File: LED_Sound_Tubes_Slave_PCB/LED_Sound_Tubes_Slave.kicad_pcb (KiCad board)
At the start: 2 copper layers, 111.9 x 52.1 mm, 50 parts, among them IC1 4050D, J2 Teensy_3_2_Header, P1 POWER + DATA, P10 LED_STR_4, P11 LED_STR_5, P2 +5V, P3 0V, P4 +5V, P5 0V, P6 LED_STR_1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

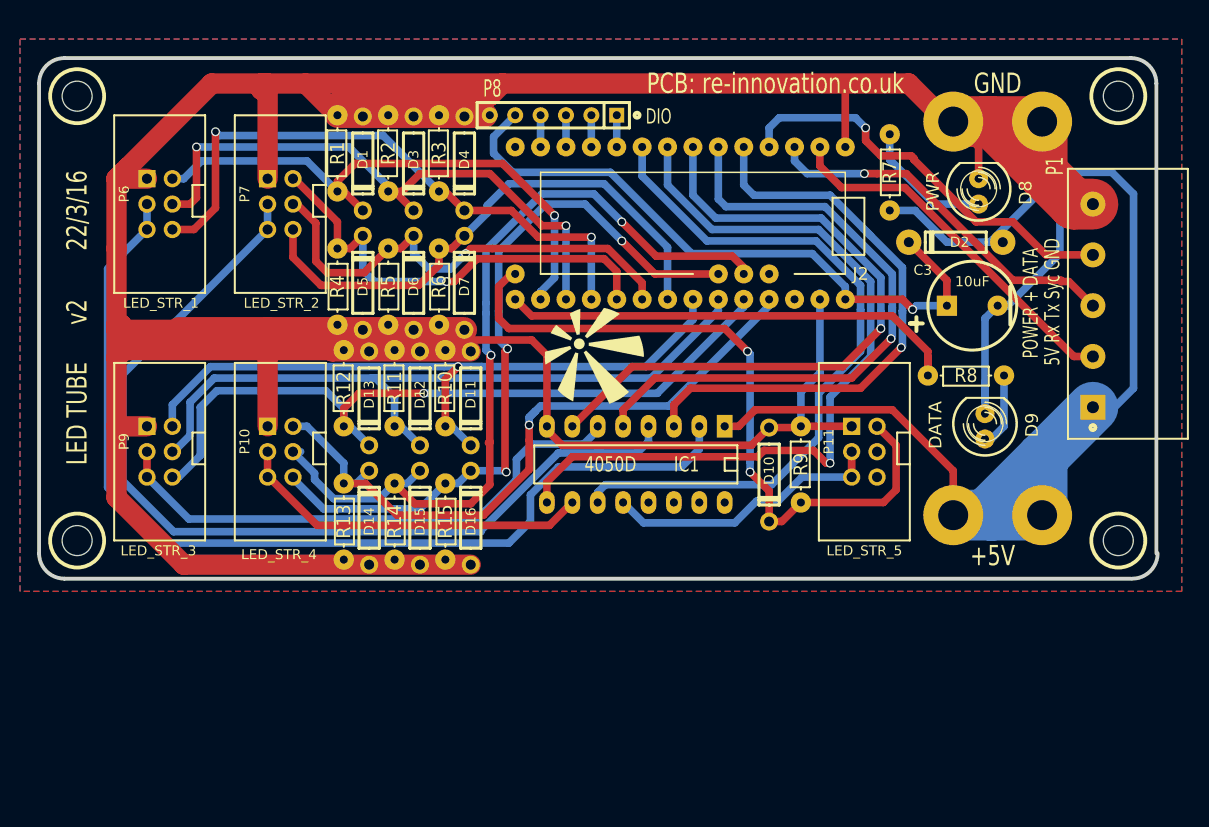
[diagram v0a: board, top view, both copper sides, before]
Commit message: New PCB with filters
Added filters. Total redesign of PCB
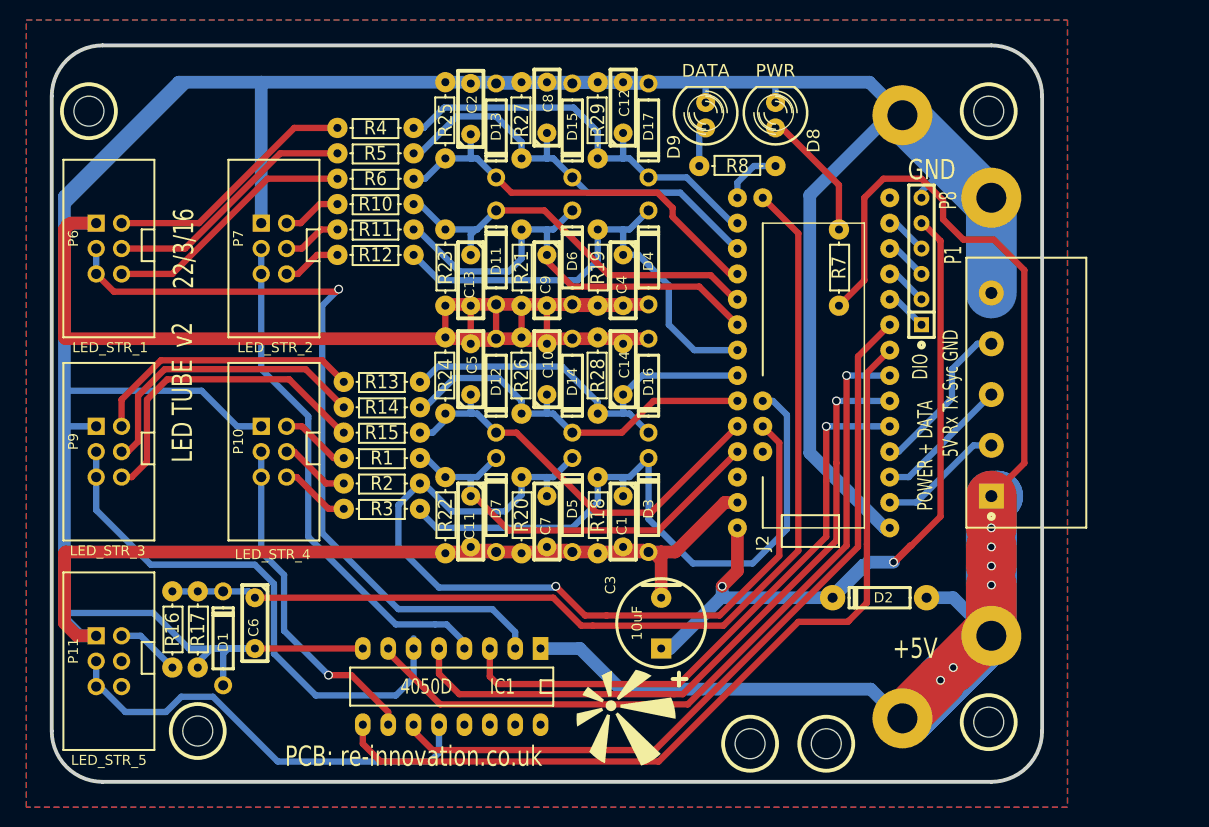
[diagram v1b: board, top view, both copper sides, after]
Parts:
- removed D10: 5V1 Diode, REInnovationFootprint:TH_Diode_3
- removed R9: 1M, REInnovationFootprint:TH_Resistor_1
- added C1: 100n, matts_components:C1_wide_lg_pad, F.Cu at (138.4, 104.8)
- added C10: 100n, matts_components:C1_wide_lg_pad, F.Cu at (130.8, 92.1)
- added C11: 100n, matts_components:C1_wide_lg_pad, F.Cu at (123.2, 104.8)
- added C12: 100n, matts_components:C1_wide_lg_pad, F.Cu at (138.4, 65.9)
- added C13: 100n, matts_components:C1_wide_lg_pad, F.Cu at (123.2, 80.6)
- added C14: 100n, matts_components:C1_wide_lg_pad, F.Cu at (138.4, 92.1)
- added C2: 100n, matts_components:C1_wide_lg_pad, F.Cu at (123.2, 66.0)
- added C4: 100n, matts_components:C1_wide_lg_pad, F.Cu at (138.4, 80.6)
- added C5: 100n, matts_components:C1_wide_lg_pad, F.Cu at (123.2, 92.1)
- added C6: 100n, matts_components:C1_wide_lg_pad, F.Cu at (101.6, 114.9)
- added C7: 100n, matts_components:C1_wide_lg_pad, F.Cu at (130.8, 104.8)
- added C8: 100n, matts_components:C1_wide_lg_pad, F.Cu at (130.8, 65.9)
- added C9: 100n, matts_components:C1_wide_lg_pad, F.Cu at (130.8, 80.6)
- added D17: 5V1 Diode, REInnovationFootprint:TH_Diode_3, F.Cu at (141.0, 66.5)
- added MH5: CONN_1, REInnovationFootprint:3mm_hole, F.Cu at (158.8, 128.3)
- added MH6: CONN_1, REInnovationFootprint:3mm_hole, F.Cu at (151.1, 128.3)
- added R16: 1k, REInnovationFootprint:TH_Resistor_1, F.Cu at (93.3, 116.8)
- added R17: 1M, REInnovationFootprint:TH_Resistor_1, F.Cu at (95.9, 116.8)
- added R18: 1M, REInnovationFootprint:TH_Resistor_1, F.Cu at (135.9, 105.4)
- added R19: 1M, REInnovationFootprint:TH_Resistor_1, F.Cu at (135.9, 80.6)
- added R20: 1M, REInnovationFootprint:TH_Resistor_1, F.Cu at (128.3, 105.4)
- added R21: 1M, REInnovationFootprint:TH_Resistor_1, F.Cu at (128.3, 80.6)
- added R22: 1M, REInnovationFootprint:TH_Resistor_1, F.Cu at (120.7, 105.4)
- added R23: 1M, REInnovationFootprint:TH_Resistor_1, F.Cu at (120.7, 80.6)
- added R24: 1M, REInnovationFootprint:TH_Resistor_1, F.Cu at (120.7, 91.4)
- added R25: 1M, REInnovationFootprint:TH_Resistor_1, F.Cu at (120.7, 65.9)
- added R26: 1M, REInnovationFootprint:TH_Resistor_1, F.Cu at (128.3, 91.4)
- added R27: 1M, REInnovationFootprint:TH_Resistor_1, F.Cu at (128.3, 65.9)
- added R28: 1M, REInnovationFootprint:TH_Resistor_1, F.Cu at (135.9, 91.4)
- added R29: 1M, REInnovationFootprint:TH_Resistor_1, F.Cu at (135.9, 65.9)
- J2: footprint TH_Teensy-3.1 -> REInnovationFootprint:TH_Teensy-3.1
- R1, R10, R11, R12, R13, R14, R15, R2, R3, R4, R5, R6: value 1M -> 1k
- moved P11 78.4 mm to (87.0, 120.0)
- moved D1 50.2 mm to (98.4, 118.1), turned to 90 degrees
- moved C3 44.5 mm to (142.2, 116.2), turned to 90 degrees
- moved D15 42.3 mm to (133.3, 66.5), turned to 270 degrees
- moved D3 42.1 mm to (141.0, 104.8), turned to 90 degrees
- moved D9 41.8 mm to (146.7, 65.4)
- moved P8 39.6 mm to (168.3, 80.0), turned to 90 degrees
- moved D2 36.4 mm to (164.5, 113.7)
- moved LG1 36.3 mm to (139.1, 126.4)
- moved J2 36.2 mm to (165.1, 104.1), turned to 90 degrees
- moved R3 36.0 mm to (114.3, 104.8), turned to 180 degrees
- moved R2 33.0 mm to (114.3, 102.2), turned to 180 degrees
- moved R8 31.0 mm to (149.9, 70.5), turned to 0 degrees
- moved R1 30.8 mm to (114.3, 99.7), turned to 180 degrees
- moved D5 30.5 mm to (133.3, 104.8)
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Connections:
- D1 pad 1: PIEZO1 -> PIEZO13
- D11 pad 1: PIEZO7 -> PIEZO4
- D12 pad 1: PIEZO8 -> PIEZO9
- D13 pad 1: PIEZO9 -> PIEZO3
- D14 pad 1: PIEZO10 -> PIEZO8
- D15 pad 1: PIEZO11 -> PIEZO2
- D16 pad 1: PIEZO12 -> PIEZO7
- D3 pad 1: PIEZO2 -> PIEZO12
- D4 pad 1: PIEZO3 -> PIEZO6
- D5 pad 1: PIEZO4 -> PIEZO11
- D7 pad 1: PIEZO6 -> PIEZO10
- P10 pad 2: PIEZO10 -> Net-(P10-Pad2)
- P10 pad 4: PIEZO11 -> Net-(P10-Pad4)
- P10 pad 6: PIEZO12 -> Net-(P10-Pad6)
- P11 pad 2: PIEZO13 -> Net-(P11-Pad2)
- P6 pad 2: PIEZO1 -> Net-(P6-Pad2)
- P6 pad 4: PIEZO2 -> Net-(P6-Pad4)
- P6 pad 6: PIEZO3 -> Net-(P6-Pad6)
- P7 pad 2: PIEZO4 -> Net-(P7-Pad2)
- P7 pad 4: PIEZO5 -> Net-(P7-Pad4)
- P7 pad 6: PIEZO6 -> Net-(P7-Pad6)
- P9 pad 2: PIEZO7 -> Net-(P9-Pad2)
- P9 pad 4: PIEZO8 -> Net-(P9-Pad4)
- P9 pad 6: PIEZO9 -> Net-(P9-Pad6)
- R1 pad 1: PIEZO1 -> PIEZO10
- R1 pad 2: GND -> Net-(P10-Pad2)
- R10 pad 1: PIEZO7 -> PIEZO4
- R10 pad 2: GND -> Net-(P7-Pad2)
- R11 pad 1: PIEZO8 -> PIEZO5
- R11 pad 2: GND -> Net-(P7-Pad4)
- R12 pad 1: PIEZO9 -> PIEZO6
- R12 pad 2: GND -> Net-(P7-Pad6)
- R13 pad 1: PIEZO10 -> PIEZO7
- R13 pad 2: GND -> Net-(P9-Pad2)
- R14 pad 1: PIEZO11 -> PIEZO8
- R14 pad 2: GND -> Net-(P9-Pad4)
- R15 pad 1: PIEZO12 -> PIEZO9
- R15 pad 2: GND -> Net-(P9-Pad6)
- R2 pad 1: PIEZO2 -> PIEZO11
- R2 pad 2: GND -> Net-(P10-Pad4)
- R3 pad 1: PIEZO3 -> PIEZO12
- R3 pad 2: GND -> Net-(P10-Pad6)
- R4 pad 1: PIEZO4 -> PIEZO1
- R4 pad 2: GND -> Net-(P6-Pad2)
- R5 pad 1: PIEZO5 -> PIEZO2
- R5 pad 2: GND -> Net-(P6-Pad4)
- R6 pad 1: PIEZO6 -> PIEZO3
- R6 pad 2: GND -> Net-(P6-Pad6)
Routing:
- net GND: track 593.1 -> 832.5 mm
- net +5V: track 121.6 -> 174.4 mm, vias 0 -> 6
- net Net-(IC1-Pad4): track 94.8 -> 51.8 mm
- net Net-(J2-Pad13): track 47.1 -> 6.02 mm
- net PIEZO8: track 72.9 -> 39.4 mm
- net PIEZO9: track 76.1 -> 42.8 mm, vias 1 -> 0
- net PIEZO13: track 70.7 -> 103.9 mm, vias 2 -> 0
- net Net-(P9-Pad6): track 0.00 -> 32.1 mm
- net PIEZO7: track 72.0 -> 41.5 mm, vias 1 -> 0
- net Net-(P9-Pad4): track 0.00 -> 29.9 mm
- net Net-(P9-Pad2): track 0.00 -> 27.4 mm
- net PIEZO10: track 68.8 -> 42.7 mm, vias 1 -> 0
- net Net-(P6-Pad6): track 0.00 -> 25.5 mm
- net Net-(P6-Pad2): track 0.00 -> 25.5 mm
- net Net-(P6-Pad4): track 0.00 -> 25.5 mm
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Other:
- board size 111.9 x 52.1 mm -> 99.1 x 73.7 mm
- net class Default: trace_width 2.032 -> 1.27
